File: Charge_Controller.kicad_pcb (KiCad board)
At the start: 2 copper layers, 134.6 x 76.2 mm, 146 parts, among them J1 SOLAR, J10 Conn_01x01_Female, J11 Conn_01x01_Female, J12 Conn_01x01_Female, J13 Conn_01x01_Female, J14 Conn_01x01_Female, J15 Conn_01x01_Female, J16 Conn_01x01_Female, J17 Conn_01x01_Female, J18 Conn_01x01_Female, J19 Conn_01x01_Female, J2 Conn_01x01_Female, J20 Conn_01x01_Female, J21 Conn_01x01_Female, J22 Conn_01x01_Female, J23 Conn_01x01_Female, J24 Conn_01x01_Female, J25 Conn_01x01_Female, J26 Conn_01x01_Female, J27 Conn_01x01_Female, J28 Conn_01x01_Female, J29 Conn_01x01_Female, J3 Conn_01x01_Female, J30 Conn_01x01_Female, J31 Conn_01x01_Female, J32 Conn_01x01_Female, J36 FAN, J37 I2C_CON, J38 I2C_CON, J4 Conn_01x01_Female, J5 Conn_01x01_Female, J6 Conn_01x01_Female, J7 Conn_01x01_Female, J8 BATT, J9 USB_OTG, Q1 CSD19505, Q2 CSD19505, Q3 CSD19505, Q4 Si2306, Q5 2N3904, Q6 2N3904, Q7 PMOS-100V-78A, Q8 PMOS-100V-78A, Q9 Si2306, SW1 RIGHT, SW2 LEFT, SW3 BACK, SW4 SELECT, U1 ACS712-30A, U10 ADS1015, U11 NUP4202, U2 B1212, U3 AMS1117-5.0, U4 AMS1117-3.3, U5 XL7005A, U6 XL7005A, U7 IR2104, U8 ESP32-WROOM-32, U9 CH340C

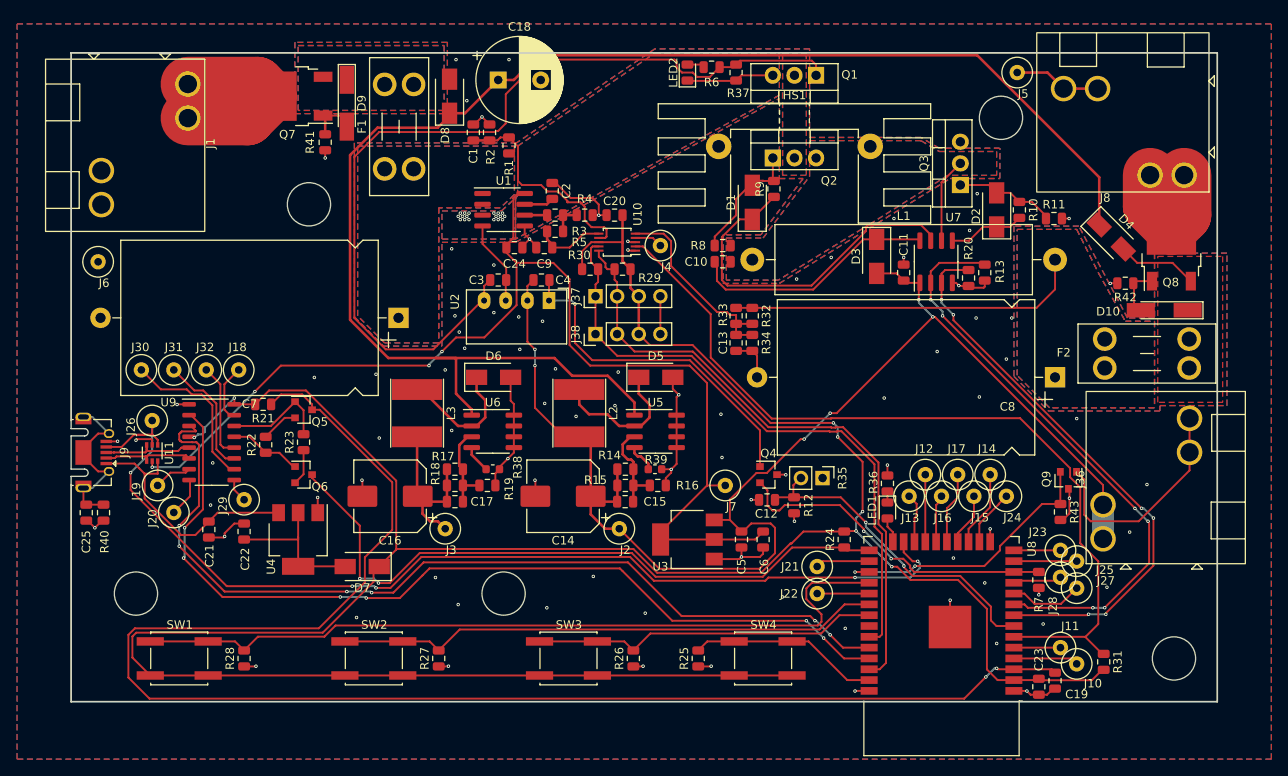
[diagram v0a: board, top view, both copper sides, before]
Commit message: Draft, no more courtyard problems, all traces connected
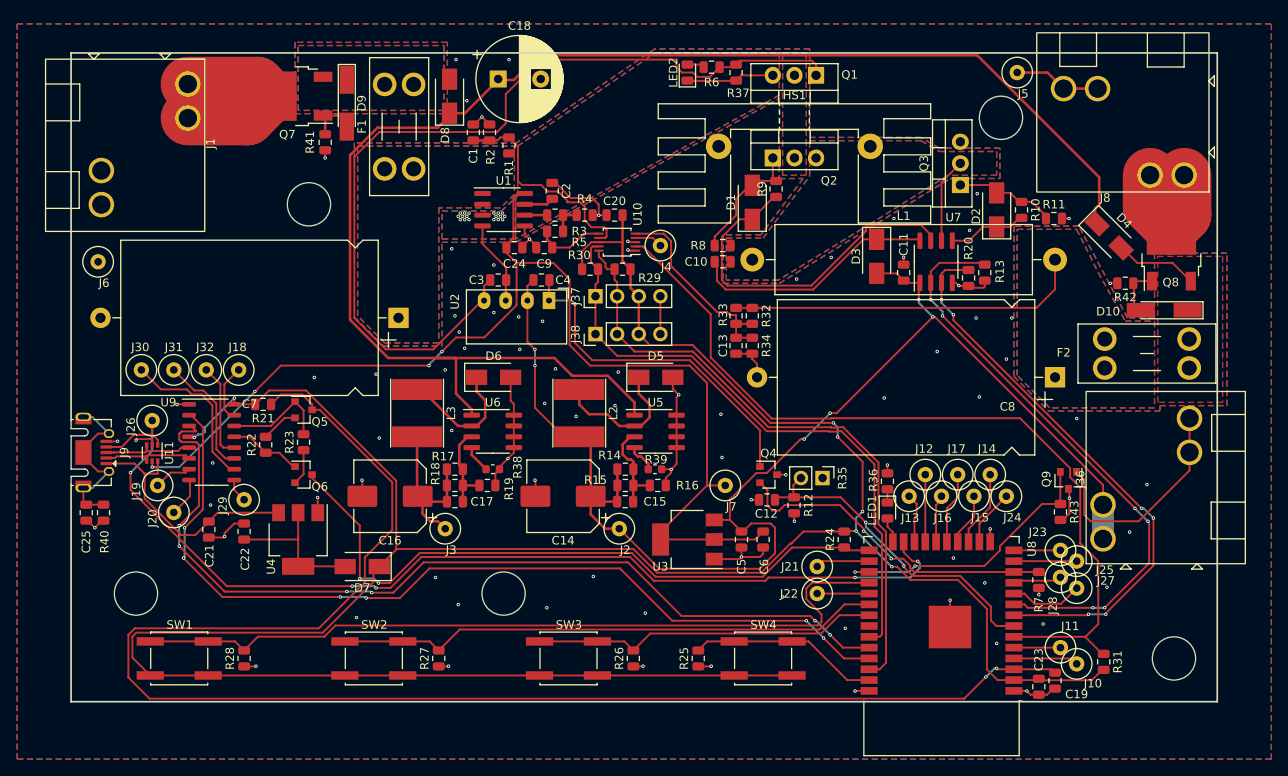
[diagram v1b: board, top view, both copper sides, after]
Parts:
- moved C13 0.33 mm to (144.6, 102.2)
- moved R34 0.33 mm to (146.5, 102.2)
- moved D4 0.28 mm to (188.4, 89.3)
- moved R36 0.25 mm to (162.3, 118.2)
- moved R10 0.25 mm to (178.1, 86.3)
- moved R9 0.25 mm to (149.3, 83.8)
- moved C18 0.11 mm to (116.6, 70.9)
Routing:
- net Net-(D2-Pad2): track 12.5 -> 11.9 mm

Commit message: R0.1 almost done draft.
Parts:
- removed J37: I2C_CON, Connector_PinHeader_2.54mm:PinHeader_1x04_P2.54mm_Vertical
- added C26: 100nf, Capacitor_SMD:C_0805_2012Metric, F.Cu at (119.7, 125.4)
- added C27: 100nf, Capacitor_SMD:C_0805_2012Metric, F.Cu at (136.3, 137.5)
- added DS1: LCD, LCD:LCD_LCM-S01602DTR_A, F.Cu at (106.0, 118.9)
- added J33: Conn_01x01_Female, TestPoint:TestPoint_Loop_D3.50mm_Drill0.9mm_Beaded, F.Cu at (176.9, 74.6)
- added J34: Conn_01x01_Female, TestPoint:TestPoint_Loop_D3.50mm_Drill0.9mm_Beaded, F.Cu at (70.3, 92.4)
- added R46: 10k, Resistor_SMD:R_0805_2012Metric, F.Cu at (125.5, 131.8)
- added R47: 10k, Resistor_SMD:R_0805_2012Metric, F.Cu at (127.4, 131.2)
- added R48: 10k, Resistor_SMD:R_0805_2012Metric, F.Cu at (126.1, 128.6)
- added R49: 330, Resistor_SMD:R_0805_2012Metric, F.Cu at (109.6, 131.8)
- added RV1: 10k, Potentiometer_SMD:Potentiometer_Bourns_3314G_Vertical, F.Cu at (150.4, 133.0)
- added U12: PCF8574, Package_SO:SSOP-20_4.4x6.5mm_P0.65mm, F.Cu at (119.7, 130.0)
- LOGO1: moved to F.Cu
- moved J6 17.6 mm to (85.5, 84.8)
- moved C18 5.77 mm to (121.1, 74.6), turned to 35 degrees
- moved R32 3.04 mm to (149.3, 97.5)
- moved R33 3.04 mm to (147.3, 97.5)
- moved C13 3.04 mm to (147.3, 101.0)
- moved R34 3.04 mm to (149.3, 101.0)
- moved R25 1.57 mm to (140.1, 140.5)
- moved R26 1.57 mm to (132.5, 140.5)
- moved R27 1.57 mm to (109.6, 140.5)
- moved R28 1.57 mm to (86.8, 140.5)
- moved SW1 1.57 mm to (79.2, 140.5)
- moved SW2 1.57 mm to (102.0, 140.5)
- moved SW3 1.57 mm to (124.9, 140.5)
- moved SW4 1.57 mm to (147.7, 140.5)
- turned LOGO1 to 0 degrees
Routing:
- net +3.3VA: track 319.2 -> 394.4 mm, vias 7 -> 9
- net /SDA: track 72.7 -> 127.6 mm, vias 0 -> 2
- net /SCL: track 74.3 -> 124.6 mm, vias 0 -> 2
- net /S+: track 20.8 -> 0.00 mm, vias 0 -> 170
- net Net-(RV1-Pad2): track 0.00 -> 18.9 mm
- net /S+B+1A: track 173.1 -> 191.3 mm
- net Net-(U12-Pad10): track 0.00 -> 15.3 mm, vias 0 -> 1
- net Net-(U12-Pad12): track 0.00 -> 14.7 mm, vias 0 -> 1
- net /B+: track 14.0 -> 0.00 mm, vias 0 -> 131
- net Net-(U12-Pad11): track 0.00 -> 13.8 mm, vias 0 -> 1
- net Net-(U12-Pad9): track 0.00 -> 13.6 mm, vias 0 -> 1
- net /RW: track 0.00 -> 10.5 mm, vias 0 -> 1
- net /E: track 0.00 -> 8.27 mm, vias 0 -> 1
- net /TX: track 106.8 -> 114.8 mm
- net Net-(DS1-Pad15): track 0.00 -> 7.65 mm
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- added copper zone on B.Cu, net /B+
- added copper zone on F.Cu, net /B+
- added copper zone on B.Cu, net /B+Polarity
- added copper zone on B.Cu, net /S+
- added copper zone on F.Cu, net /S+
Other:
- outline, holes or cut-outs redrawn
- board text added: "1"
- board text added: "2"
- board text added: "R0.1"

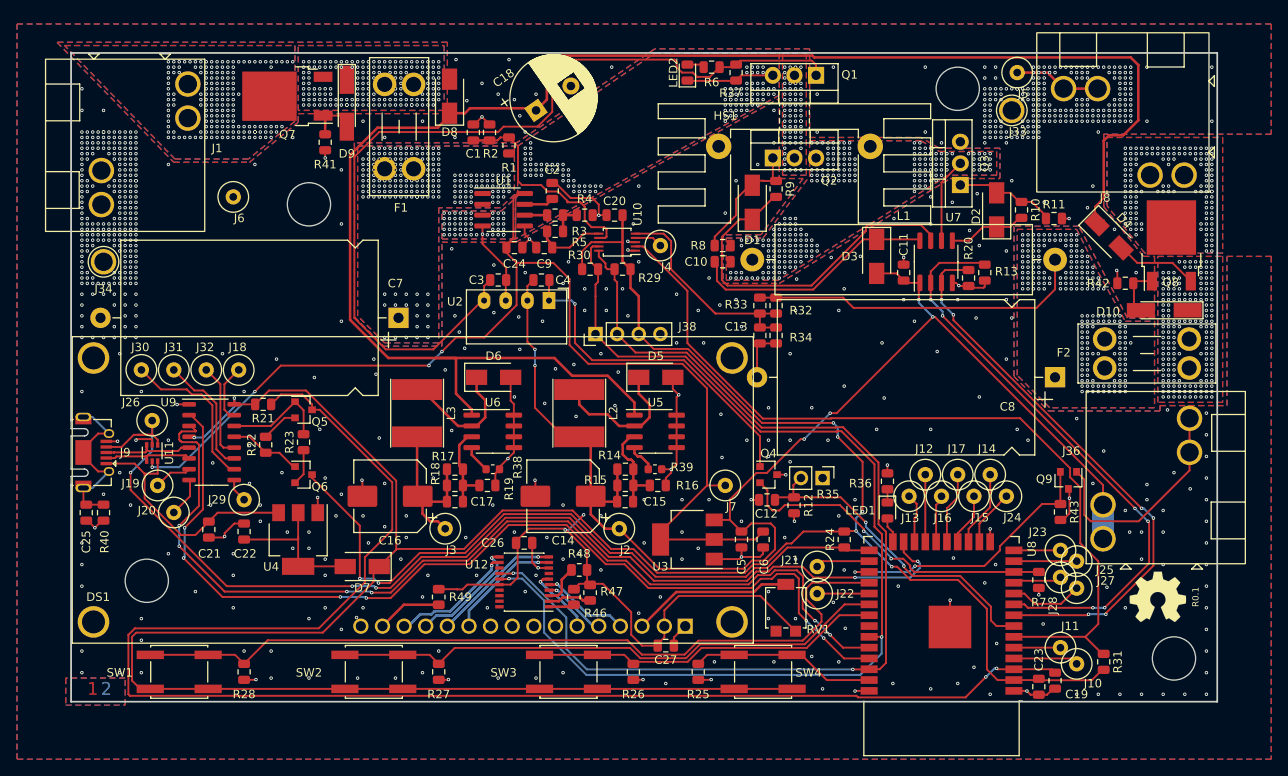
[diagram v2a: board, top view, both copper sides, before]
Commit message: Added a bit of silk screen.
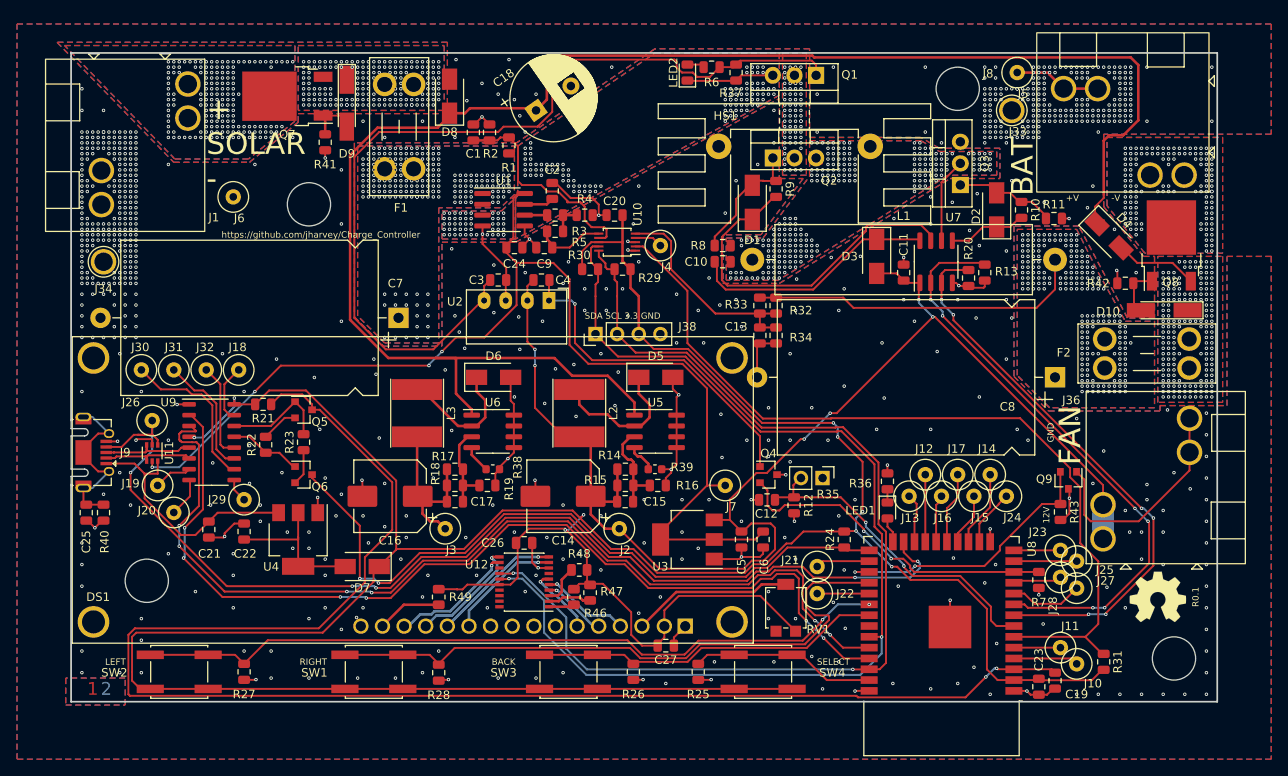
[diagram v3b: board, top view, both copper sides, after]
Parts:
- moved R28 22.9 mm to (109.6, 140.6)
- moved R27 22.9 mm to (86.8, 140.5)
- moved SW1 22.9 mm to (102.0, 140.5)
- moved SW2 22.9 mm to (79.2, 140.5)
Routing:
- net /PB_LFT: track 65.9 -> 89.2 mm, vias 0 -> 2
- net /PB-RHT: track 95.0 -> 73.8 mm
- net /S+: vias 170 -> 169
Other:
- board text added: "+ SOLAR -"
- board text added: "+V"
- board text added: "-V"
- board text added: "12V"
- board text added: "BACK"
- board text added: "BAT"
- board text added: "FAN"
- board text added: "GND"
- board text added: "LEFT"
- board text added: "RIGHT"
- board text added: "SDA SCL 3.3 GND"
- board text added: "SELECT"
- board text added: "https://github.com/jharvey/Charge_Controller"
